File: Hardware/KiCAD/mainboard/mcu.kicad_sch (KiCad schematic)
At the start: 15 parts, among them U1 STM32F405RGTx, Y1 8 MHz

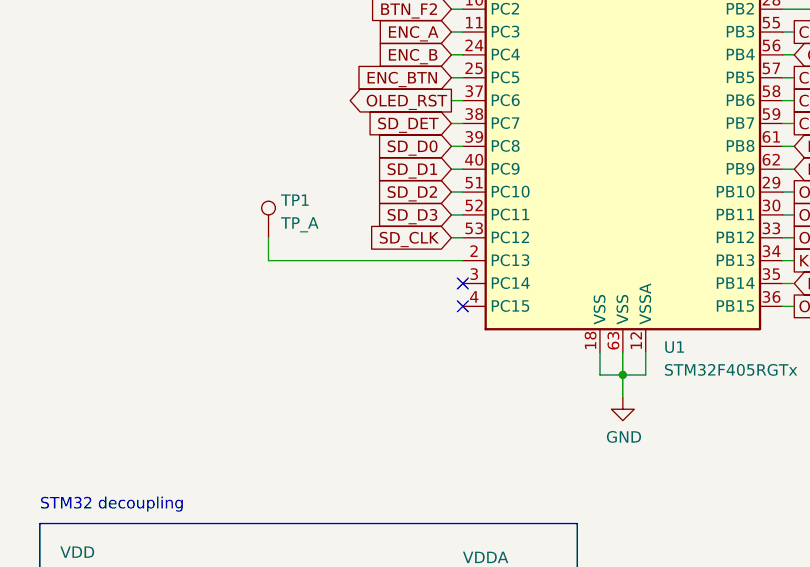
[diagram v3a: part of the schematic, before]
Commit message: Add ANY_KEY signal from keypad.
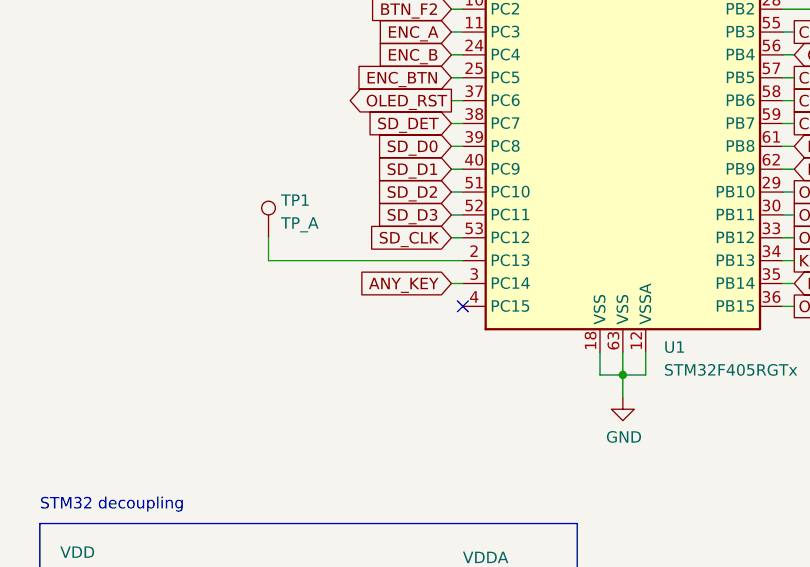
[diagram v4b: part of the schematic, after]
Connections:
- net ANY_KEY: now reaches U1.3 (PC14)
- no-connect marks 4 -> 3
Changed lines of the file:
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@@
   (junction (at 60.96 167.64) (diameter 1.016) (color 0 0 0 0)
   )
-  (no_connect (at 132.08 129.54))
   (no_connect (at 132.08 132.08))
   (no_connect (at 167.64 71.12))
@@
   )
   (wire (pts (xy 130.81 88.9) (xy 132.08 88.9))
+    (stroke (width 0) (type default) (color 0 0 0 0))
+  )
+  (wire (pts (xy 130.81 129.54) (xy 132.08 129.54))
     (stroke (width 0) (type default) (color 0 0 0 0))
   )
@@
       (effects (font (size 1.27 1.27)) (justify right) hide)
     )
+  )
+  (global_label "ANY_KEY" (shape input) (at 130.81 129.54 180) (fields_autoplaced)
+    (effects (font (size 1.27 1.27)) (justify right))
+    (property "Intersheet References" "${INTERSHEET_REFS}" (id 0) (at 120.414 129.4606 0)
+      (effects (font (size 1.27 1.27)) (justify right) hide)
+    )
